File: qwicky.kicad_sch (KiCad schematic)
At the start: 44 parts, among them J1 Conn_02x05_Odd_Even, J2 Conn_01x02, J3 Conn_01x02, J4 Conn_01x04, J5 Conn_01x02, J6 Conn_01x02, U1 STM32F405RGT6, U2 AMS1117-3.3

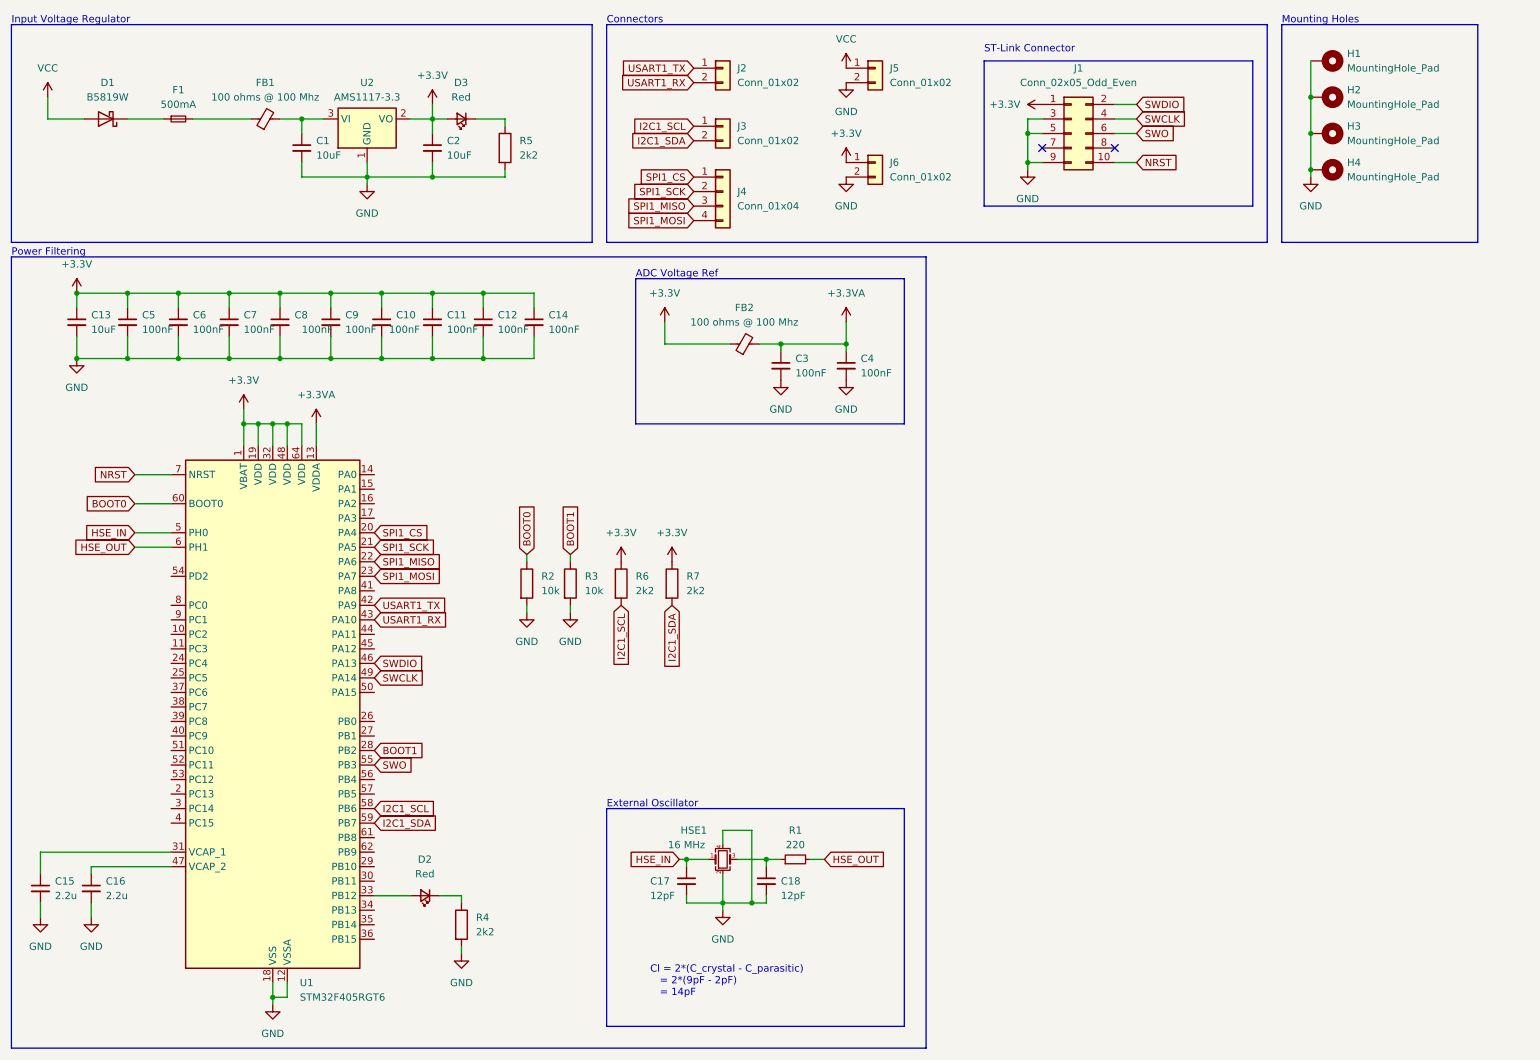
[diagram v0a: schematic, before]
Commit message: Upgraded chip to STM32F407VETx. Added STM32CubeMX files.
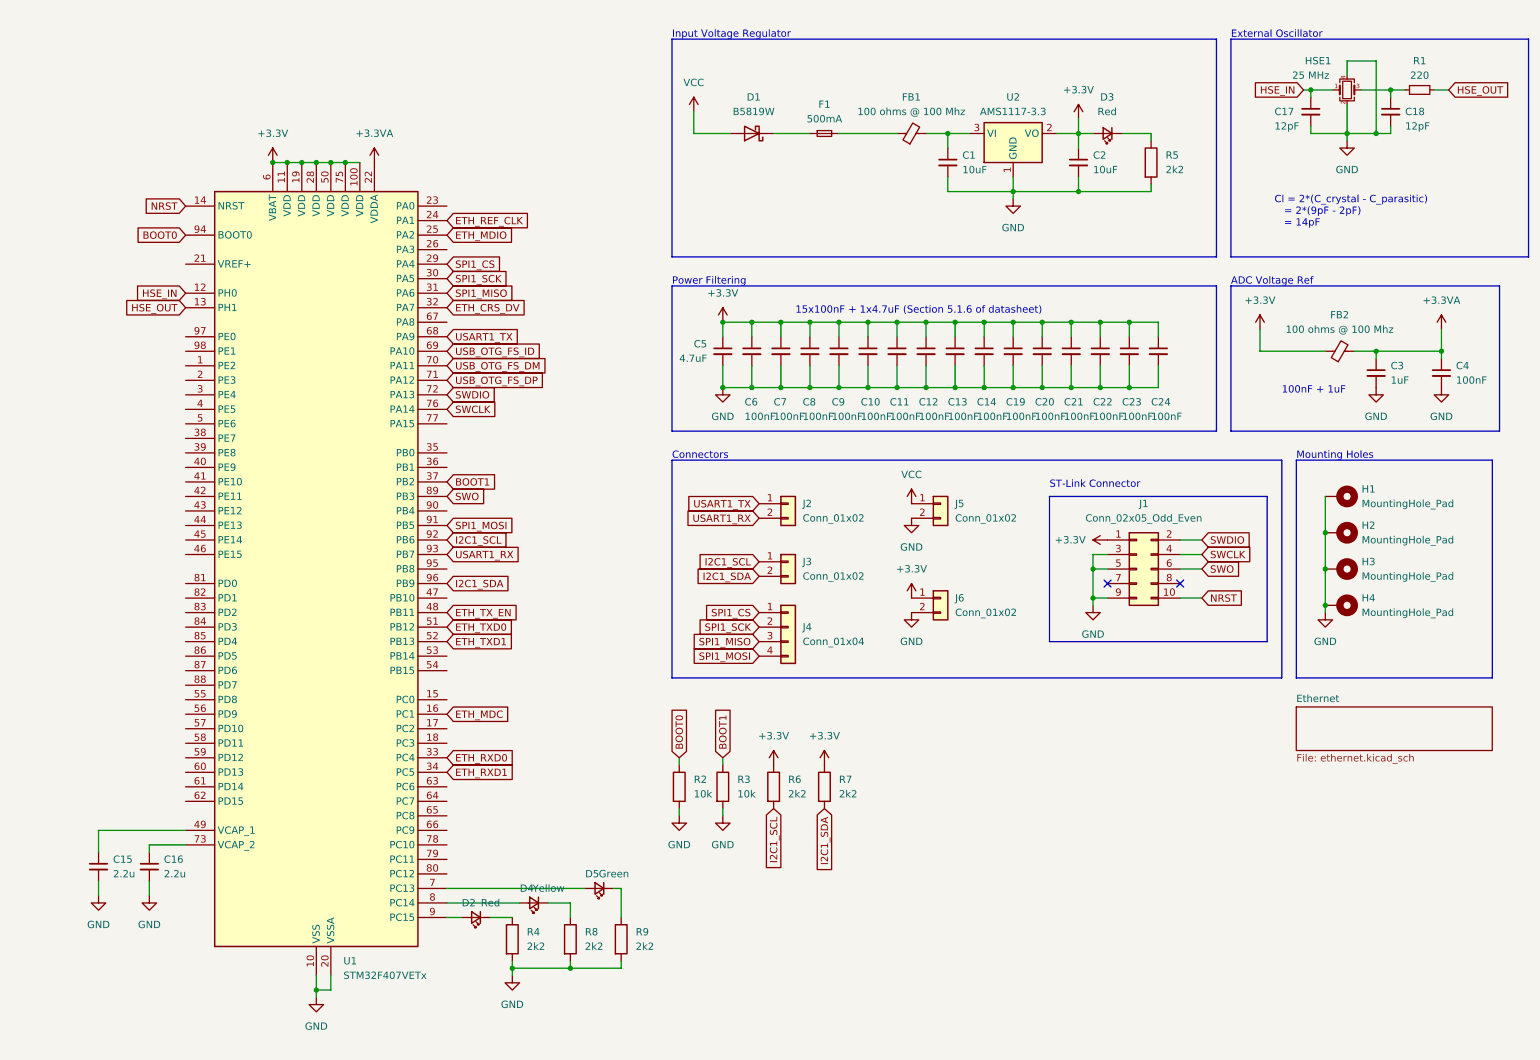
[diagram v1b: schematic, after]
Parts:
- removed U1: STM32F405RGT6, Package_QFP:LQFP-64_10x10mm_P0.5mm, symbol MCU_ST_STM32F4:STM32F405RGTx
- added C19, C20, C21, C22, C23, C24: 100nF, symbol Device:C_Small
- added D4: Yellow, symbol Device:LED_Small
- added D5: Green, symbol Device:LED_Small
- added R8, R9: 2k2, symbol Device:R
- added U1: STM32F407VETx, Package_QFP:LQFP-100_14x14mm_P0.5mm, symbol MCU_ST_STM32F4:STM32F407VETx
- C13: value 10uF -> 100nF
- C3: value 100nF -> 1uF
- C5: value 100nF -> 4.7uF
- HSE1: value 16 MHz -> 25 MHz
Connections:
- net +3.3V: now also C19.1, C20.1, C21.1, C22.1, C23.1, C24.1, U1.100 (VDD), U1.11 (VDD), U1.19 (VDD), U1.28 (VDD), U1.50 (VDD), U1.6 (VBAT), U1.75 (VDD)
- net +3.3VA: now also U1.22 (VDDA)
- net BOOT0: now also U1.94 (BOOT0)
- net BOOT1: now also U1.37 (PB2)
- net GND: now also C19.2, C20.2, C21.2, C22.2, C23.2, C24.2, R8.2, R9.2, U1.10 (VSS), U1.20 (VSSA), U1.27 (VSS), U1.74 (VSS), U1.99 (VSS)
- net HSE_IN: now also U1.12 (PH0)
- net HSE_OUT: now also U1.13 (PH1)
- net I2C1_SCL: now also U1.92 (PB6)
- net I2C1_SDA: now also U1.96 (PB9)
- net NRST: now also U1.14 (NRST)
- net SPI1_CS: now also U1.29 (PA4)
- net SPI1_MISO: now also U1.31 (PA6)
- net SPI1_MOSI: now also U1.91 (PB5)
- net SPI1_SCK: now also U1.30 (PA5)
- net SWCLK: now also U1.76 (PA14)
- net SWDIO: now also U1.72 (PA13)
- net SWO: now also U1.89 (PB3)
- net USART1_RX: now also U1.93 (PB7)
- net USART1_TX: now also U1.68 (PA9)
- net at D2.2 (A): now also U1.9 (PC15)
- net at C15.1: now also U1.49 (VCAP_1)
- net at C16.1: now also U1.73 (VCAP_2)
- new net: D4.1 (K), R8.1
- new net: D5.2 (A), U1.7 (PC13)
- new net: D4.2 (A), U1.8 (PC14)
- new net: D5.1 (K), R9.1
- new net ETH_CRS_DV: U1.32 (PA7)
- new net ETH_MDC: U1.16 (PC1)
- new net ETH_MDIO: U1.25 (PA2)
- new net ETH_REF_CLK: U1.24 (PA1)
- new net ETH_RXD0: U1.33 (PC4)
- new net ETH_RXD1: U1.34 (PC5)
- new net ETH_TXD0: U1.51 (PB12)
- new net ETH_TXD1: U1.52 (PB13)
- new net ETH_TX_EN: U1.48 (PB11)
- new net USB_OTG_FS_DM: U1.70 (PA11)
- new net USB_OTG_FS_DP: U1.71 (PA12)
- new net USB_OTG_FS_ID: U1.69 (PA10)
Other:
- added sheet Ethernet (ethernet.kicad_sch)
- note added: "100nF + 1uF"
- note added: "15x100nF + 1x4.7uF (Section 5.1.6 of datasheet)"
- moved on the sheet: C1, C15, C16, C17, C18, C2, C3, C4, D1, D2, D3, F1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

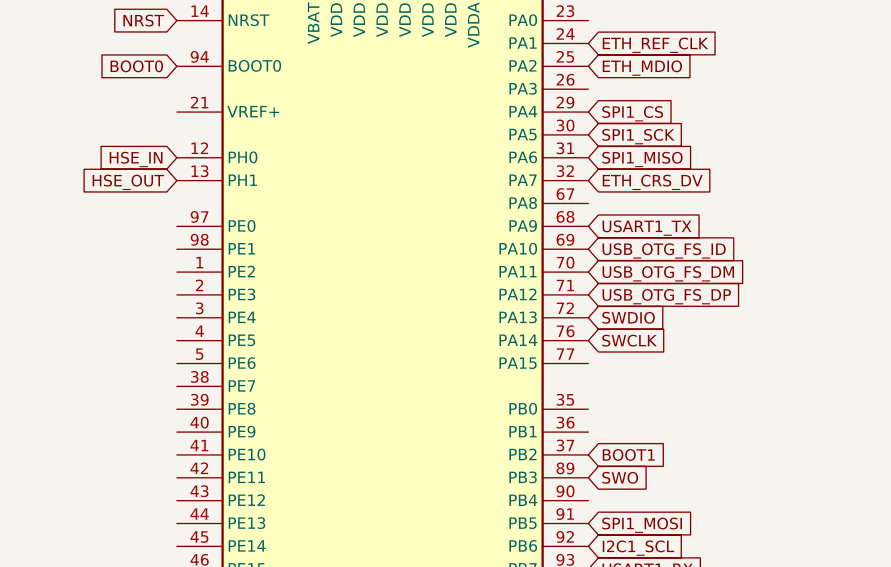
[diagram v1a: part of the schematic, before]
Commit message: Working on ethernet schematic
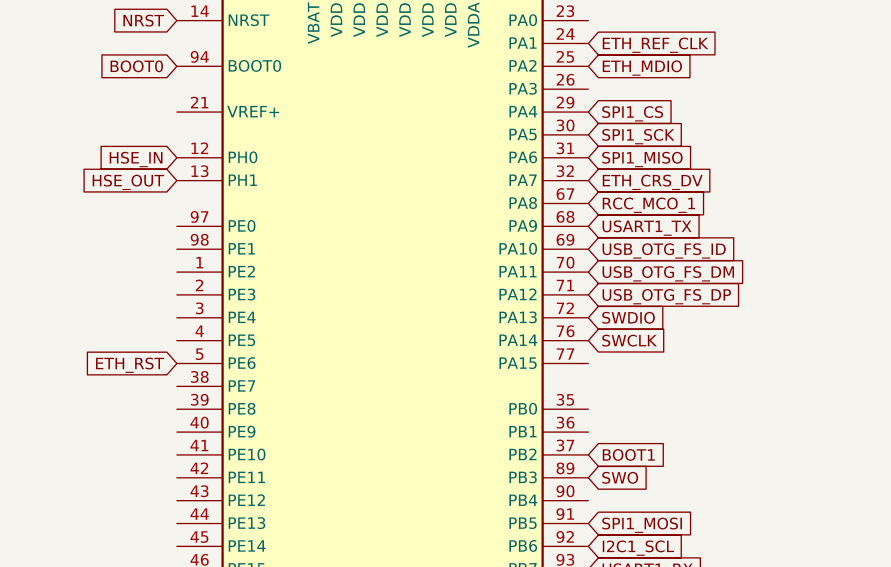
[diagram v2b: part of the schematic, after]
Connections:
- net ETH_RST: now reaches U1.5 (PE6)
- net RCC_MCO_1: now reaches U1.67 (PA8)
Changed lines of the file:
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@@
+    )
+  )
+  (global_label "ETH_RST" (shape input) (at 44.45 85.09 180) (fields_autoplaced)
+    (effects (font (size 1.27 1.27)) (justify right))
+    (property "Intersheetrefs" "${INTERSHEET_REFS}" (at 33.603 85.09 0)
+      (effects (font (size 1.27 1.27)) (justify right) hide)
     )
   )
@@
       (effects (font (size 1.27 1.27)) (justify left) hide)
     )
+  )
+  (global_label "RCC_MCO_1" (shape input) (at 90.17 67.31 0) (fields_autoplaced)
+    (effects (font (size 1.27 1.27)) (justify left))
+    (property "Intersheetrefs" "${INTERSHEET_REFS}" (at 104.1618 67.31 0)
+      (effects (font (size 1.27 1.27)) (justify left) hide)
+    )

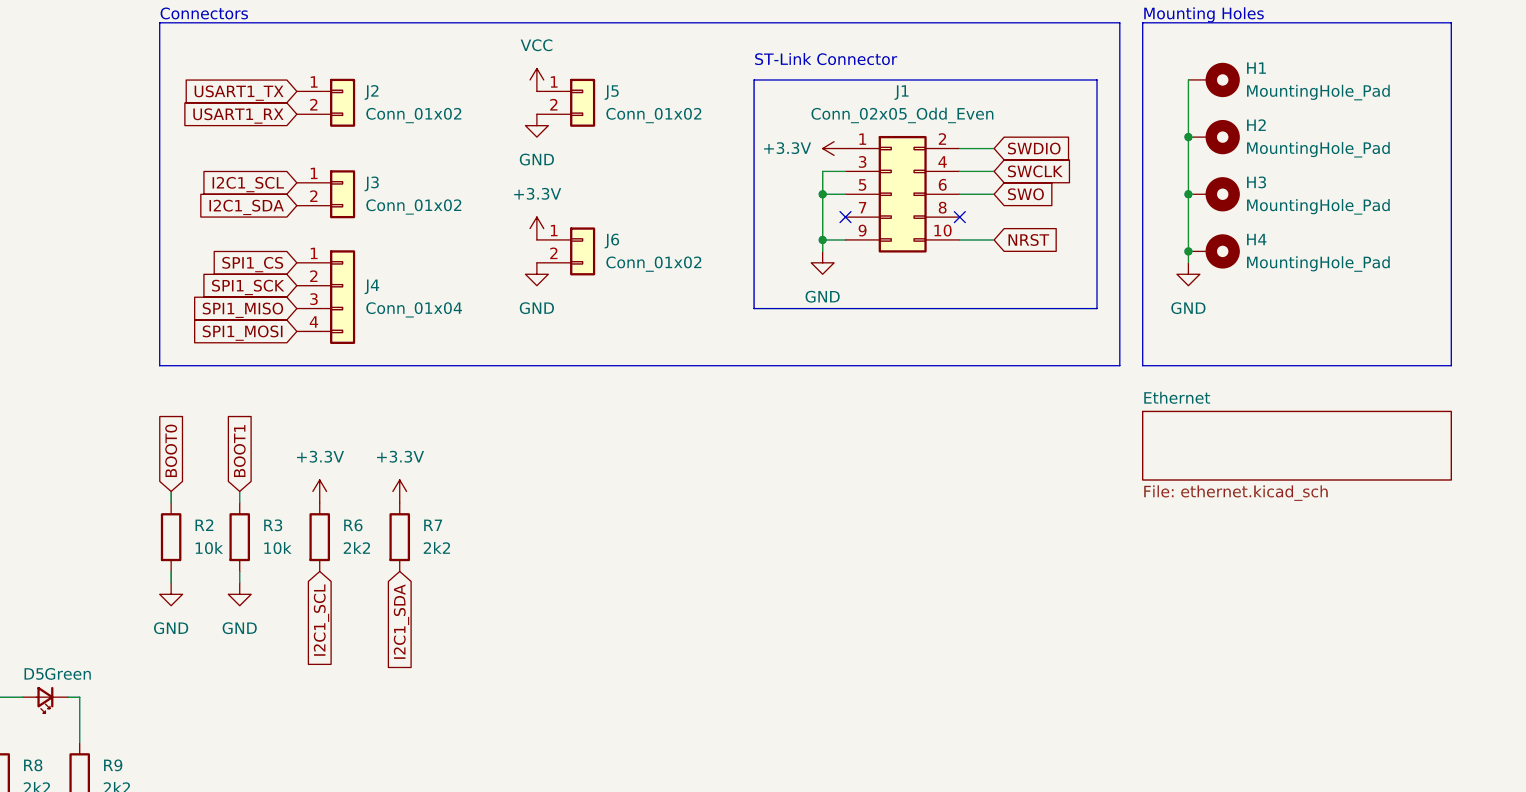
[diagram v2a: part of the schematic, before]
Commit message: Added SSD1306 display with schematic libraries from https://github.com/MichMich/KiCad-SSD1306_OLED-0.91-128x32
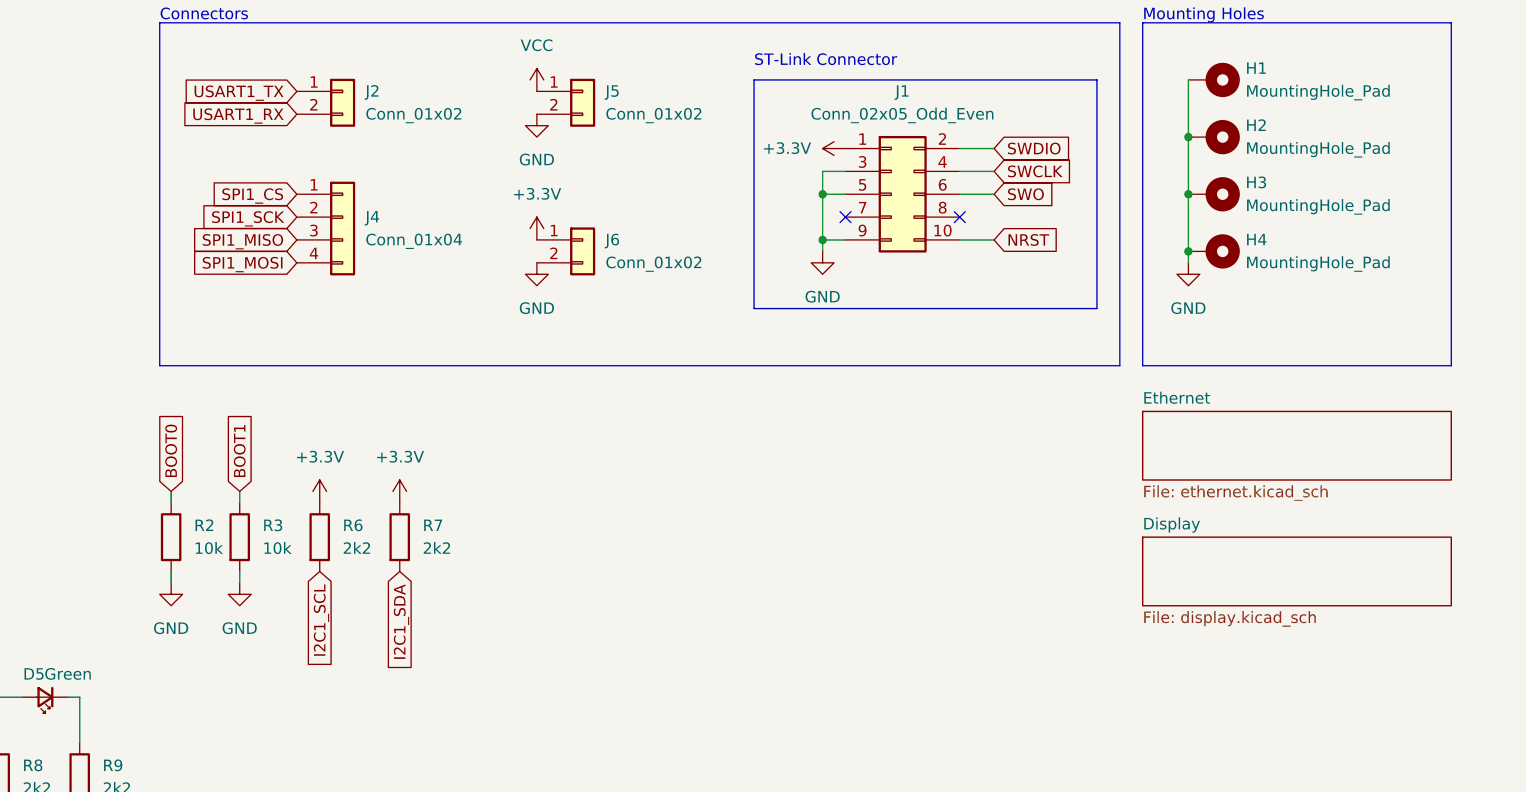
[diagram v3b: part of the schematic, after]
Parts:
- removed J3: Conn_01x02, symbol Connector_Generic:Conn_01x02
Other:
- added sheet Display (display.kicad_sch)
- moved on the sheet: J4
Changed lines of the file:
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@@
     )
   )
-  (global_label "SPI1_SCK" (shape input) (at 144.78 120.65 180) (fields_autoplaced)
+  (global_label "SPI1_SCK" (shape input) (at 144.78 113.03 180) (fields_autoplaced)
     (effects (font (size 1.27 1.27)) (justify right))
-    (property "Intersheetrefs" "${INTERSHEET_REFS}" (at 132.7839 120.65 0)
+    (property "Intersheetrefs" "${INTERSHEET_REFS}" (at 132.7839 113.03 0)
       (effects (font (size 1.27 1.27)) (justify right) hide)
     )
   )
-  (global_label "SPI1_MISO" (shape input) (at 144.78 123.19 180) (fields_autoplaced)
+  (global_label "SPI1_MISO" (shape input) (at 144.78 115.57 180) (fields_autoplaced)
     (effects (font (size 1.27 1.27)) (justify right))
-    (property "Intersheetrefs" "${INTERSHEET_REFS}" (at 131.9372 123.19 0)
-      (effects (font (size 1.27 1.27)) (justify right) hide)
-    )
-  )
-  (global_label "I2C1_SDA" (shape input) (at 144.78 111.76 180) (fields_autoplaced)
-    (effects (font (size 1.27 1.27)) (justify right))
-    (property "Intersheetrefs" "${INTERSHEET_REFS}" (at 132.9653 111.76 0)
+    (property "Intersheetrefs" "${INTERSHEET_REFS}" (at 131.9372 115.57 0)
       (effects (font (size 1.27 1.27)) (justify right) hide)
     )
@@
     )
   )
-  (global_label "I2C1_SCL" (shape input) (at 144.78 109.22 180) (fields_autoplaced)
-    (effects (font (size 1.27 1.27)) (justify right))
-    (property "Intersheetrefs" "${INTERSHEET_REFS}" (at 133.0258 109.22 0)
-      (effects (font (size 1.27 1.27)) (justify right) hide)
-    )
-  )
   (global_label "SWO" (shape input) (at 90.17 97.79 0) (fields_autoplaced)
     (effects (font (size 1.27 1.27)) (justify left))
@@
     )
   )
-  (global_label "SPI1_CS" (shape input) (at 144.78 118.11 180) (fields_autoplaced)
+  (global_label "SPI1_CS" (shape input) (at 144.78 110.49 180) (fields_autoplaced)
     (effects (font (size 1.27 1.27)) (justify right))
-    (property "Intersheetrefs" "${INTERSHEET_REFS}" (at 134.0539 118.11 0)
+    (property "Intersheetrefs" "${INTERSHEET_REFS}" (at 134.0539 110.49 0)
       (effects (font (size 1.27 1.27)) (justify right) hide)
     )
@@
     )
   )
-  (global_label "SPI1_MOSI" (shape input) (at 144.78 125.73 180) (fields_autoplaced)
+  (global_label "SPI1_MOSI" (shape input) (at 144.78 118.11 180) (fields_autoplaced)
     (effects (font (size 1.27 1.27)) (justify right))
-    (property "Intersheetrefs" "${INTERSHEET_REFS}" (at 131.9372 125.73 0)
+    (property "Intersheetrefs" "${INTERSHEET_REFS}" (at 131.9372 118.11 0)
       (effects (font (size 1.27 1.27)) (justify right) hide)
     )
@@
     )
   )
-  (symbol (lib_id "Connector_Generic:Conn_01x04") (at 149.86 120.65 0) (unit 1)
-    (in_bom yes) (on_board yes) (dnp no) (fields_autoplaced)
-    (property "Reference" "J4" (at 152.4 120.65 0)
-      (effects (font (size 1.27 1.27)) (justify left))
-    )
-    (property "Value" "Conn_01x04" (at 152.4 123.19 0)
-      (effects (font (size 1.27 1.27)) (justify left))
-    )
-    (property "Footprint" "" (at 149.86 120.65 0)
-      (effects (font (size 1.27 1.27)) hide)
-    )
-    (property "Datasheet" "~" (at 149.86 120.65 0)
+  (symbol (lib_id "Connector_Generic:Conn_01x04") (at 149.86 113.03 0) (unit 1)
+    (in_bom yes) (on_board yes) (dnp no) (fields_autoplaced)
+    (property "Reference" "J4" (at 152.4 113.03 0)
+      (effects (font (size 1.27 1.27)) (justify left))
+    )
+    (property "Value" "Conn_01x04" (at 152.4 115.57 0)
+      (effects (font (size 1.27 1.27)) (justify left))
+    )
+    (property "Footprint" "" (at 149.86 113.03 0)
+      (effects (font (size 1.27 1.27)) hide)
+    )
+    (property "Datasheet" "~" (at 149.86 113.03 0)
       (effects (font (size 1.27 1.27)) hide)
     )
@@
     )
   )
-  (symbol (lib_id "Connector_Generic:Conn_01x02") (at 149.86 109.22 0) (unit 1)
-    (in_bom yes) (on_board yes) (dnp no) (fields_autoplaced)
-    (property "Reference" "J3" (at 152.4 109.22 0)
-      (effects (font (size 1.27 1.27)) (justify left))
-    )
-    (property "Value" "Conn_01x02" (at 152.4 111.76 0)
-      (effects (font (size 1.27 1.27)) (justify left))
-    )
-    (property "Footprint" "" (at 149.86 109.22 0)
-      (effects (font (size 1.27 1.27)) hide)
-    )
-    (property "Datasheet" "~" (at 149.86 109.22 0)
-      (effects (font (size 1.27 1.27)) hide)
-    )
-    (pin "1")
-    (pin "2")
-    (instances
-      (project "qwicky"
-        (path "/bd74968a-27d8-4281-bec5-c611f9e7fcfb"
-          (reference "J3") (unit 1)
-        )
-      )
-    )
-  )
   (symbol (lib_id "power:GND") (at 252.73 78.74 0) (unit 1)
     (in_bom yes) (on_board yes) (dnp no) (fields_autoplaced)
@@
       )
     )
+  )
+  (sheet (at 238.76 148.59) (size 34.29 7.62) (fields_autoplaced)
+    (stroke (width 0.1524) (type solid))
+    (fill (color 0 0 0 0.0000))
+    (property "Sheetname" "Display" (at 238.76 147.8784 0)
+      (effects (font (size 1.27 1.27)) (justify left bottom))
+    )
+    (property "Sheetfile" "display.kicad_sch" (at 238.76 156.7946 0)
+      (effects (font (size 1.27 1.27)) (justify left top))
+    )
+    (instances
+      (project "qwicky"
+        (path "/bd74968a-27d8-4281-bec5-c611f9e7fcfb" (page "3"))
+      )
+    )
